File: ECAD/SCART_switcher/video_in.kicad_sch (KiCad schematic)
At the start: 32 parts, among them U48 TS5A63157DBV, U49 TS5A63157DBV, U52 TS5A63157DBV, U53 TS5A63157DBV

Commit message: progressed ECAD.
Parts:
- renumbered U48 to U49, U49 to U50, U52 to U53, U53 to U54

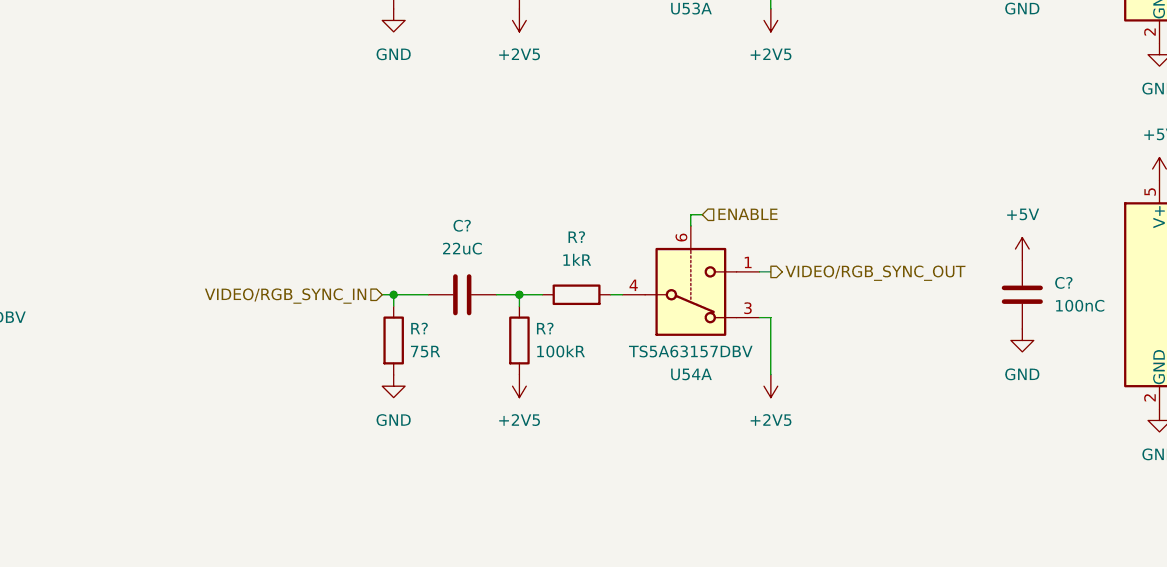
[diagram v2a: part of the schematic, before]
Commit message: ERC fixes.
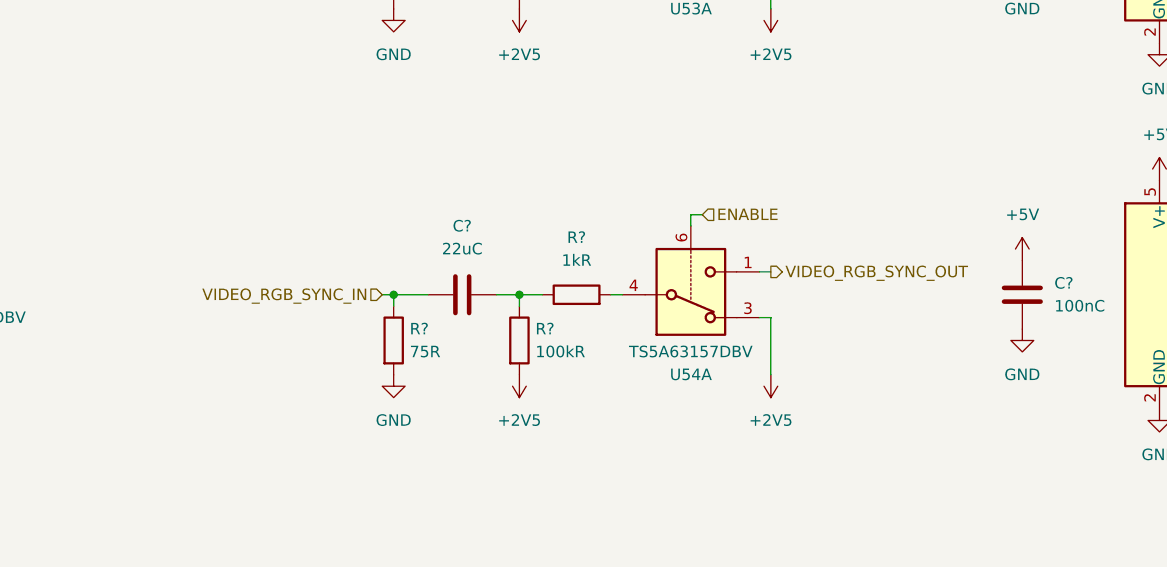
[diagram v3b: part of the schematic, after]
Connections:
- net VIDEO/RGB_SYNC_IN renamed VIDEO_RGB_SYNC_IN
- net VIDEO/RGB_SYNC_OUT renamed VIDEO_RGB_SYNC_OUT

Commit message: Progressed ECAD. Error fixing and cleanup.
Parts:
- renumbered U49 to U48, U50 to U49, U53 to U52, U54 to U53

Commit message: Progressed ECAD.
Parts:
- Q?: MFN BC847B,215 -> (none); MPN (none) -> BC847B,215
- R? (x2): MPN (none) -> RC0805FR-0710KL
- U?: MFN 74AHC1G126W5-7 -> (none); MPN (none) -> 74AHC1G126W5-7
- U?: MFN 74AHC1G14SE-7 -> (none); MPN (none) -> 74AHC1G14SE-7
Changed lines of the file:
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@@
       (effects (font (size 1.27 1.27)) hide)
     )
-    (property "MFN" "" (at 43.18 90.17 0)
-      (effects (font (size 1.27 1.27)) hide)
-    )
     (pin "1")
     (pin "2")
@@
       (effects (font (size 1.27 1.27)) hide)
     )
-    (property "MFN" "" (at 36.83 43.18 0)
-      (effects (font (size 1.27 1.27)) hide)
-    )
     (pin "1")
     (pin "2")
@@
       (effects (font (size 1.27 1.27)) hide)
     )
-    (property "Datasheet" "~" (at 110.49 139.7 0)
+    (property "Datasheet" "https://datasheet.lcsc.com/lcsc/1810201611_YAGEO-RC0805FR-0710KL_C84376.pdf" (at 110.49 139.7 0)
+      (effects (font (size 1.27 1.27)) hide)
+    )
+    (property "MPN" "RC0805FR-0710KL" (at 110.49 139.7 0)
       (effects (font (size 1.27 1.27)) hide)
     )
@@
       (effects (font (size 1.27 1.27)) hide)
     )
-    (property "MFN" "" (at 29.21 48.26 0)
-      (effects (font (size 1.27 1.27)) hide)
-    )
     (pin "1")
     (pin "2")
@@
       (effects (font (size 1.27 1.27)) hide)
     )
-    (property "MFN" "" (at 91.44 154.94 0)
-      (effects (font (size 1.27 1.27)) hide)
-    )
     (pin "1")
     (pin "2")
@@
       (effects (font (size 1.27 1.27)) hide)
     )
-    (property "MFN" "" (at 173.99 48.26 0)
-      (effects (font (size 1.27 1.27)) hide)
-    )
     (pin "1")
     (pin "2")
@@
       (effects (font (size 1.27 1.27)) hide)
     )
-    (property "MFN" "" (at 187.96 88.9 0)
-      (effects (font (size 1.27 1.27)) hide)
-    )
     (pin "1")
     (pin "2")
@@
       (effects (font (size 1.27 1.27)) hide)
     )
-    (property "MFN" "" (at 99.06 85.09 0)
-      (effects (font (size 1.27 1.27)) hide)
-    )
     (property "MPN" "CL21B104KBCNNNC" (at 99.06 85.09 0)
       (effects (font (size 1.27 1.27)) hide)
@@
       (effects (font (size 1.27 1.27)) hide)
     )
-    (property "MFN" "" (at 196.85 143.51 0)
-      (effects (font (size 1.27 1.27)) hide)
-    )
     (property "MPN" "CL21B104KBCNNNC" (at 196.85 143.51 0)
       (effects (font (size 1.27 1.27)) hide)
@@
       (effects (font (size 1.27 1.27)) (justify left) hide)
     )
-    (property "MFN" "BC847B,215" (at 107.95 148.59 0)
+    (property "MPN" "BC847B,215" (at 107.95 148.59 0)
       (effects (font (size 1.27 1.27)) hide)
     )
@@
       (effects (font (size 1.27 1.27)) hide)
     )
-    (property "MFN" "" (at 43.18 48.26 0)
-      (effects (font (size 1.27 1.27)) hide)
-    )
     (pin "1")
     (pin "2")
@@
       (effects (font (size 1.27 1.27)) hide)
     )
-    (property "MFN" "" (at 173.99 88.9 0)
-      (effects (font (size 1.27 1.27)) hide)
-    )
     (pin "1")
     (pin "2")
@@
       (effects (font (size 1.27 1.27)) hide)
     )
-    (property "MFN" "" (at 187.96 48.26 0)
-      (effects (font (size 1.27 1.27)) hide)
-    )
     (pin "1")
     (pin "2")
@@
       (effects (font (size 1.27 1.27)) hide)
     )
-    (property "MFN" "" (at 181.61 43.18 0)
-      (effects (font (size 1.27 1.27)) hide)
-    )
     (pin "1")
     (pin "2")
@@
       (effects (font (size 1.27 1.27)) hide)
     )
-    (property "Datasheet" "~" (at 99.06 148.59 0)
+    (property "Datasheet" "https://datasheet.lcsc.com/lcsc/1810201611_YAGEO-RC0805FR-0710KL_C84376.pdf" (at 99.06 148.59 0)
+      (effects (font (size 1.27 1.27)) hide)
+    )
+    (property "MPN" "RC0805FR-0710KL" (at 99.06 148.59 0)
       (effects (font (size 1.27 1.27)) hide)
     )
@@
       (effects (font (size 1.27 1.27)) hide)
     )
-    (property "MFN" "" (at 210.82 143.51 0)
-      (effects (font (size 1.27 1.27)) hide)
-    )
     (property "MPN" "CL21B104KBCNNNC" (at 210.82 143.51 0)
       (effects (font (size 1.27 1.27)) hide)
@@
       (effects (font (size 1.27 1.27)) hide)
     )
-    (property "MFN" "" (at 243.84 43.18 0)
-      (effects (font (size 1.27 1.27)) hide)
-    )
     (property "MPN" "CL21B104KBCNNNC" (at 243.84 43.18 0)
       (effects (font (size 1.27 1.27)) hide)
@@
       (effects (font (size 1.27 1.27)) hide)
     )
-    (property "MFN" "74AHC1G126W5-7" (at 161.29 143.51 0)
+    (property "MPN" "74AHC1G126W5-7" (at 161.29 143.51 0)
       (effects (font (size 1.27 1.27)) hide)
     )
@@
       (effects (font (size 1.27 1.27)) hide)
     )
-    (property "MFN" "" (at 243.84 83.82 0)
-      (effects (font (size 1.27 1.27)) hide)
-    )
     (property "MPN" "CL21B104KBCNNNC" (at 243.84 83.82 0)
       (effects (font (size 1.27 1.27)) hide)
@@
       (effects (font (size 1.27 1.27)) hide)
     )
-    (property "MFN" "" (at 36.83 85.09 0)
-      (effects (font (size 1.27 1.27)) hide)
-    )
     (pin "1")
     (pin "2")
@@
       (effects (font (size 1.27 1.27)) hide)
     )
-    (property "MFN" "" (at 29.21 90.17 0)
-      (effects (font (size 1.27 1.27)) hide)
-    )
     (pin "1")
     (pin "2")
@@
       (effects (font (size 1.27 1.27)) hide)
     )
-    (property "MFN" "" (at 99.06 43.18 0)
-      (effects (font (size 1.27 1.27)) hide)
-    )
     (property "MPN" "CL21B104KBCNNNC" (at 99.06 43.18 0)
       (effects (font (size 1.27 1.27)) hide)
@@
       (effects (font (size 1.27 1.27)) hide)
     )
-    (property "MFN" "74AHC1G14SE-7" (at 133.35 143.51 0)
+    (property "MPN" "74AHC1G14SE-7" (at 133.35 143.51 0)
       (effects (font (size 1.27 1.27)) hide)
     )
@@
       (effects (font (size 1.27 1.27)) hide)
     )
-    (property "MFN" "" (at 181.61 83.82 0)
-      (effects (font (size 1.27 1.27)) hide)
-    )

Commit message: Progressed ECAD.
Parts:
- renumbered U48 to U55, U49 to U56, U52 to U59, U53 to U60

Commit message: Progressed ECAD.
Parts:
- C? (x6): footprint Capacitor_SMD:C_0805_2012Metric_Pad1.18x1.45mm_HandSolder -> Capacitor_SMD:C_0805_2012Metric
- R? (x10): footprint Resistor_SMD:R_0805_2012Metric_Pad1.20x1.40mm_HandSolder -> Resistor_SMD:R_0805_2012Metric
- R? (x5): footprint Resistor_SMD:R_1210_3225Metric_Pad1.30x2.65mm_HandSolder -> Resistor_SMD:R_1210_3225Metric
- U?: footprint Package_TO_SOT_SMD:SOT-353_SC-70-5_Handsoldering -> Package_TO_SOT_SMD:SOT-353_SC-70-5
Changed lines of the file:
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@@
       (effects (font (size 1.27 1.27)))
     )
-    (property "Footprint" "Resistor_SMD:R_0805_2012Metric_Pad1.20x1.40mm_HandSolder" (at 194.31 85.598 90)
+    (property "Footprint" "Resistor_SMD:R_0805_2012Metric" (at 194.31 85.598 90)
       (effects (font (size 1.27 1.27)) hide)
     )
@@
       (effects (font (size 1.27 1.27)) (justify left))
     )
-    (property "Footprint" "Resistor_SMD:R_0805_2012Metric_Pad1.20x1.40mm_HandSolder" (at 41.402 90.17 90)
+    (property "Footprint" "Resistor_SMD:R_0805_2012Metric" (at 41.402 90.17 90)
       (effects (font (size 1.27 1.27)) hide)
     )
@@
       (effects (font (size 1.27 1.27)) (justify left))
     )
-    (property "Footprint" "Resistor_SMD:R_0805_2012Metric_Pad1.20x1.40mm_HandSolder" (at 108.712 139.7 90)
+    (property "Footprint" "Resistor_SMD:R_0805_2012Metric" (at 108.712 139.7 90)
       (effects (font (size 1.27 1.27)) hide)
     )
@@
       (effects (font (size 1.27 1.27)))
     )
-    (property "Footprint" "Resistor_SMD:R_0805_2012Metric_Pad1.20x1.40mm_HandSolder" (at 49.53 86.868 90)
+    (property "Footprint" "Resistor_SMD:R_0805_2012Metric" (at 49.53 86.868 90)
       (effects (font (size 1.27 1.27)) hide)
     )
@@
       (effects (font (size 1.27 1.27)) (justify left))
     )
-    (property "Footprint" "Resistor_SMD:R_1210_3225Metric_Pad1.30x2.65mm_HandSolder" (at 27.432 48.26 90)
+    (property "Footprint" "Resistor_SMD:R_1210_3225Metric" (at 27.432 48.26 90)
       (effects (font (size 1.27 1.27)) hide)
     )
@@
       (effects (font (size 1.27 1.27)) (justify left))
     )
-    (property "Footprint" "Resistor_SMD:R_1210_3225Metric_Pad1.30x2.65mm_HandSolder" (at 89.662 154.94 90)
+    (property "Footprint" "Resistor_SMD:R_1210_3225Metric" (at 89.662 154.94 90)
       (effects (font (size 1.27 1.27)) hide)
     )
@@
       (effects (font (size 1.27 1.27)) (justify left))
     )
-    (property "Footprint" "Resistor_SMD:R_1210_3225Metric_Pad1.30x2.65mm_HandSolder" (at 172.212 48.26 90)
+    (property "Footprint" "Resistor_SMD:R_1210_3225Metric" (at 172.212 48.26 90)
       (effects (font (size 1.27 1.27)) hide)
     )
@@
       (effects (font (size 1.27 1.27)) (justify left))
     )
-    (property "Footprint" "Resistor_SMD:R_0805_2012Metric_Pad1.20x1.40mm_HandSolder" (at 186.182 88.9 90)
+    (property "Footprint" "Resistor_SMD:R_0805_2012Metric" (at 186.182 88.9 90)
       (effects (font (size 1.27 1.27)) hide)
     )
@@
       (effects (font (size 1.27 1.27)))
     )
-    (property "Footprint" "Resistor_SMD:R_0805_2012Metric_Pad1.20x1.40mm_HandSolder" (at 49.53 44.958 90)
+    (property "Footprint" "Resistor_SMD:R_0805_2012Metric" (at 49.53 44.958 90)
       (effects (font (size 1.27 1.27)) hide)
     )
@@
       (effects (font (size 1.27 1.27)) (justify left))
     )
-    (property "Footprint" "Capacitor_SMD:C_0805_2012Metric_Pad1.18x1.45mm_HandSolder" (at 100.0252 88.9 0)
+    (property "Footprint" "Capacitor_SMD:C_0805_2012Metric" (at 100.0252 88.9 0)
       (effects (font (size 1.27 1.27)) hide)
     )
@@
       (effects (font (size 1.27 1.27)) (justify left))
     )
-    (property "Footprint" "Capacitor_SMD:C_0805_2012Metric_Pad1.18x1.45mm_HandSolder" (at 197.8152 147.32 0)
+    (property "Footprint" "Capacitor_SMD:C_0805_2012Metric" (at 197.8152 147.32 0)
       (effects (font (size 1.27 1.27)) hide)
     )
@@
       (effects (font (size 1.27 1.27)) (justify left))
     )
-    (property "Footprint" "Resistor_SMD:R_0805_2012Metric_Pad1.20x1.40mm_HandSolder" (at 41.402 48.26 90)
+    (property "Footprint" "Resistor_SMD:R_0805_2012Metric" (at 41.402 48.26 90)
       (effects (font (size 1.27 1.27)) hide)
     )
@@
       (effects (font (size 1.27 1.27)) (justify left))
     )
-    (property "Footprint" "Resistor_SMD:R_1210_3225Metric_Pad1.30x2.65mm_HandSolder" (at 172.212 88.9 90)
+    (property "Footprint" "Resistor_SMD:R_1210_3225Metric" (at 172.212 88.9 90)
       (effects (font (size 1.27 1.27)) hide)
     )
@@
       (effects (font (size 1.27 1.27)) (justify left))
     )
-    (property "Footprint" "Resistor_SMD:R_0805_2012Metric_Pad1.20x1.40mm_HandSolder" (at 186.182 48.26 90)
+    (property "Footprint" "Resistor_SMD:R_0805_2012Metric" (at 186.182 48.26 90)
       (effects (font (size 1.27 1.27)) hide)
     )
@@
       (effects (font (size 1.27 1.27)))
     )
-    (property "Footprint" "Resistor_SMD:R_0805_2012Metric_Pad1.20x1.40mm_HandSolder" (at 99.06 146.812 90)
+    (property "Footprint" "Resistor_SMD:R_0805_2012Metric" (at 99.06 146.812 90)
       (effects (font (size 1.27 1.27)) hide)
     )
@@
       (effects (font (size 1.27 1.27)) (justify left))
     )
-    (property "Footprint" "Capacitor_SMD:C_0805_2012Metric_Pad1.18x1.45mm_HandSolder" (at 211.7852 147.32 0)
+    (property "Footprint" "Capacitor_SMD:C_0805_2012Metric" (at 211.7852 147.32 0)
       (effects (font (size 1.27 1.27)) hide)
     )
@@
       (effects (font (size 1.27 1.27)) (justify left))
     )
-    (property "Footprint" "Capacitor_SMD:C_0805_2012Metric_Pad1.18x1.45mm_HandSolder" (at 244.8052 46.99 0)
+    (property "Footprint" "Capacitor_SMD:C_0805_2012Metric" (at 244.8052 46.99 0)
       (effects (font (size 1.27 1.27)) hide)
     )
@@
       (effects (font (size 1.27 1.27)) (justify left))
     )
-    (property "Footprint" "Capacitor_SMD:C_0805_2012Metric_Pad1.18x1.45mm_HandSolder" (at 244.8052 87.63 0)
+    (property "Footprint" "Capacitor_SMD:C_0805_2012Metric" (at 244.8052 87.63 0)
       (effects (font (size 1.27 1.27)) hide)
     )
@@
       (effects (font (size 1.27 1.27)))
     )
-    (property "Footprint" "Resistor_SMD:R_0805_2012Metric_Pad1.20x1.40mm_HandSolder" (at 194.31 44.958 90)
+    (property "Footprint" "Resistor_SMD:R_0805_2012Metric" (at 194.31 44.958 90)
       (effects (font (size 1.27 1.27)) hide)
     )
@@
       (effects (font (size 1.27 1.27)) (justify left))
     )
-    (property "Footprint" "Resistor_SMD:R_1210_3225Metric_Pad1.30x2.65mm_HandSolder" (at 27.432 90.17 90)
+    (property "Footprint" "Resistor_SMD:R_1210_3225Metric" (at 27.432 90.17 90)
       (effects (font (size 1.27 1.27)) hide)
     )
@@
       (effects (font (size 1.27 1.27)) (justify left))
     )
-    (property "Footprint" "Capacitor_SMD:C_0805_2012Metric_Pad1.18x1.45mm_HandSolder" (at 100.0252 46.99 0)
+    (property "Footprint" "Capacitor_SMD:C_0805_2012Metric" (at 100.0252 46.99 0)
       (effects (font (size 1.27 1.27)) hide)
     )
@@
       (effects (font (size 1.27 1.27)))
     )
-    (property "Footprint" "Package_TO_SOT_SMD:SOT-353_SC-70-5_Handsoldering" (at 133.35 143.51 0)
+    (property "Footprint" "Package_TO_SOT_SMD:SOT-353_SC-70-5" (at 133.35 143.51 0)
       (effects (font (size 1.27 1.27)) hide)
     )

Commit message: progressed ecad
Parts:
- U55, U56, U59, U60: value TS5A63157DBV -> 74LVC1G3157; footprint Package_TO_SOT_SMD:SOT-23-6 -> Package_TO_SOT_SMD:SOT-363_SC-70-6; MPN (none) -> SN74LVC1G3157DCKR
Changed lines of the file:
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@@
       (effects (font (size 1.27 1.27)) (justify left))
     )
-    (property "Value" "TS5A63157DBV" (at 120.65 44.45 0)
+    (property "Value" "74LVC1G3157" (at 120.65 44.45 0)
       (effects (font (size 1.27 1.27)) (justify left))
     )
-    (property "Footprint" "Package_TO_SOT_SMD:SOT-23-6" (at 114.3 50.8 0)
+    (property "Footprint" "Package_TO_SOT_SMD:SOT-363_SC-70-6" (at 114.3 50.8 0)
       (effects (font (size 1.27 1.27)) hide)
     )
-    (property "Datasheet" "https://www.ti.com/lit/ds/symlink/ts5a63157.pdf" (at 114.3 43.18 0)
+    (property "Datasheet" "https://datasheet.lcsc.com/lcsc/1811031937_Texas-Instruments-SN74LVC1G3157DCKR_C38663.pdf" (at 114.3 43.18 0)
+      (effects (font (size 1.27 1.27)) hide)
+    )
+    (property "MPN" "SN74LVC1G3157DCKR" (at 114.3 43.18 0)
       (effects (font (size 1.27 1.27)) hide)
     )
@@
       (effects (font (size 1.27 1.27)))
     )
-    (property "Value" "TS5A63157DBV" (at 62.23 49.53 0)
+    (property "Value" "74LVC1G3157" (at 62.23 49.53 0)
       (effects (font (size 1.27 1.27)))
     )
-    (property "Footprint" "Package_TO_SOT_SMD:SOT-23-6" (at 62.23 38.1 0)
+    (property "Footprint" "Package_TO_SOT_SMD:SOT-363_SC-70-6" (at 62.23 38.1 0)
+      (effects (font (size 1.27 1.27)) hide)
+    )
+    (property "Datasheet" "https://datasheet.lcsc.com/lcsc/1811031937_Texas-Instruments-SN74LVC1G3157DCKR_C38663.pdf" (at 62.23 45.72 0)
       (effects (font (size 1.27 1.27)) hide)
     )
-    (property "Datasheet" "https://www.ti.com/lit/ds/symlink/ts5a63157.pdf" (at 62.23 45.72 0)
+    (property "MPN" "SN74LVC1G3157DCKR" (at 62.23 45.72 0)
       (effects (font (size 1.27 1.27)) hide)
     )
@@
       (effects (font (size 1.27 1.27)) (justify left))
     )
-    (property "Value" "TS5A63157DBV" (at 264.16 44.45 0)
+    (property "Value" "74LVC1G3157" (at 264.16 44.45 0)
       (effects (font (size 1.27 1.27)) (justify left))
     )
-    (property "Footprint" "Package_TO_SOT_SMD:SOT-23-6" (at 259.08 50.8 0)
+    (property "Footprint" "Package_TO_SOT_SMD:SOT-363_SC-70-6" (at 259.08 50.8 0)
       (effects (font (size 1.27 1.27)) hide)
     )
-    (property "Datasheet" "https://www.ti.com/lit/ds/symlink/ts5a63157.pdf" (at 259.08 43.18 0)
+    (property "Datasheet" "https://datasheet.lcsc.com/lcsc/1811031937_Texas-Instruments-SN74LVC1G3157DCKR_C38663.pdf" (at 259.08 43.18 0)
+      (effects (font (size 1.27 1.27)) hide)
+    )
+    (property "MPN" "SN74LVC1G3157DCKR" (at 259.08 43.18 0)
       (effects (font (size 1.27 1.27)) hide)
     )
@@
       (effects (font (size 1.27 1.27)) (justify left))
     )
-    (property "Value" "TS5A63157DBV" (at 119.38 86.36 0)
+    (property "Value" "74LVC1G3157" (at 119.38 86.36 0)
       (effects (font (size 1.27 1.27)) (justify left))
     )
-    (property "Footprint" "Package_TO_SOT_SMD:SOT-23-6" (at 114.3 92.71 0)
+    (property "Footprint" "Package_TO_SOT_SMD:SOT-363_SC-70-6" (at 114.3 92.71 0)
+      (effects (font (size 1.27 1.27)) hide)
+    )
+    (property "Datasheet" "https://datasheet.lcsc.com/lcsc/1811031937_Texas-Instruments-SN74LVC1G3157DCKR_C38663.pdf" (at 114.3 85.09 0)
       (effects (font (size 1.27 1.27)) hide)
     )
-    (property "Datasheet" "https://www.ti.com/lit/ds/symlink/ts5a63157.pdf" (at 114.3 85.09 0)
+    (property "MPN" "SN74LVC1G3157DCKR" (at 114.3 85.09 0)
       (effects (font (size 1.27 1.27)) hide)
     )
@@
       (effects (font (size 1.27 1.27)))
     )
-    (property "Value" "TS5A63157DBV" (at 62.23 91.44 0)
+    (property "Value" "74LVC1G3157" (at 62.23 91.44 0)
       (effects (font (size 1.27 1.27)))
     )
-    (property "Footprint" "Package_TO_SOT_SMD:SOT-23-6" (at 62.23 80.01 0)
+    (property "Footprint" "Package_TO_SOT_SMD:SOT-363_SC-70-6" (at 62.23 80.01 0)
       (effects (font (size 1.27 1.27)) hide)
     )
-    (property "Datasheet" "https://www.ti.com/lit/ds/symlink/ts5a63157.pdf" (at 62.23 87.63 0)
+    (property "Datasheet" "https://datasheet.lcsc.com/lcsc/1811031937_Texas-Instruments-SN74LVC1G3157DCKR_C38663.pdf" (at 62.23 87.63 0)
+      (effects (font (size 1.27 1.27)) hide)
+    )
+    (property "MPN" "SN74LVC1G3157DCKR" (at 62.23 87.63 0)
       (effects (font (size 1.27 1.27)) hide)
     )
@@
       (effects (font (size 1.27 1.27)))
     )
-    (property "Value" "TS5A63157DBV" (at 207.01 49.53 0)
+    (property "Value" "74LVC1G3157" (at 207.01 49.53 0)
       (effects (font (size 1.27 1.27)))
     )
-    (property "Footprint" "Package_TO_SOT_SMD:SOT-23-6" (at 207.01 38.1 0)
+    (property "Footprint" "Package_TO_SOT_SMD:SOT-363_SC-70-6" (at 207.01 38.1 0)
+      (effects (font (size 1.27 1.27)) hide)
+    )
+    (property "Datasheet" "https://datasheet.lcsc.com/lcsc/1811031937_Texas-Instruments-SN74LVC1G3157DCKR_C38663.pdf" (at 207.01 45.72 0)
       (effects (font (size 1.27 1.27)) hide)
     )
-    (property "Datasheet" "https://www.ti.com/lit/ds/symlink/ts5a63157.pdf" (at 207.01 45.72 0)
+    (property "MPN" "SN74LVC1G3157DCKR" (at 207.01 45.72 0)
       (effects (font (size 1.27 1.27)) hide)
     )
@@
       (effects (font (size 1.27 1.27)))
     )
-    (property "Value" "TS5A63157DBV" (at 207.01 90.17 0)
+    (property "Value" "74LVC1G3157" (at 207.01 90.17 0)
       (effects (font (size 1.27 1.27)))
     )
-    (property "Footprint" "Package_TO_SOT_SMD:SOT-23-6" (at 207.01 78.74 0)
+    (property "Footprint" "Package_TO_SOT_SMD:SOT-363_SC-70-6" (at 207.01 78.74 0)
       (effects (font (size 1.27 1.27)) hide)
     )
-    (property "Datasheet" "https://www.ti.com/lit/ds/symlink/ts5a63157.pdf" (at 207.01 86.36 0)
+    (property "Datasheet" "https://datasheet.lcsc.com/lcsc/1811031937_Texas-Instruments-SN74LVC1G3157DCKR_C38663.pdf" (at 207.01 86.36 0)
+      (effects (font (size 1.27 1.27)) hide)
+    )
+    (property "MPN" "SN74LVC1G3157DCKR" (at 207.01 86.36 0)
       (effects (font (size 1.27 1.27)) hide)
     )
@@
       (effects (font (size 1.27 1.27)) (justify left))
     )
-    (property "Value" "TS5A63157DBV" (at 264.16 85.09 0)
+    (property "Value" "74LVC1G3157" (at 264.16 85.09 0)
       (effects (font (size 1.27 1.27)) (justify left))
     )
-    (property "Footprint" "Package_TO_SOT_SMD:SOT-23-6" (at 259.08 91.44 0)
+    (property "Footprint" "Package_TO_SOT_SMD:SOT-363_SC-70-6" (at 259.08 91.44 0)
+      (effects (font (size 1.27 1.27)) hide)
+    )
+    (property "Datasheet" "https://datasheet.lcsc.com/lcsc/1811031937_Texas-Instruments-SN74LVC1G3157DCKR_C38663.pdf" (at 259.08 83.82 0)
       (effects (font (size 1.27 1.27)) hide)
     )
-    (property "Datasheet" "https://www.ti.com/lit/ds/symlink/ts5a63157.pdf" (at 259.08 83.82 0)
+    (property "MPN" "SN74LVC1G3157DCKR" (at 259.08 83.82 0)
       (effects (font (size 1.27 1.27)) hide)
     )
